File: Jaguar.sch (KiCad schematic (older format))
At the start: 23 parts, among them P1 12v-SW, P10 O2, P11 O2-GND, P12 TACH-IN, P13 Ground, P14 BATT-GND, P15 DIS-BYPASS, P16 IGN-ADVANCE, P17 CONN_4, P18 CONN_4, P19 INJ-GND, P2 BRV-12v, P20 12v-SW, P21 Fuel Relay+, P22 Fuel Relay-, P23 Injectors, P3 BRV-GND, P4 IAT, P5 MAT, P6 COOLANT, P7 TPS-5v, P8 TPS, P9 TPS-GND

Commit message: Redesigned schematics and board
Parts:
- removed P17, P18: CONN_4, symbol CONN_4
- added P15: CAM-IN, symbol CONN_1
- added P2: 12v-SW2, symbol CONN_1
- added P20: PT3-5, symbol CONN_3
- added P21: Inj-IN, symbol CONN_3
- added P3: 12v-SW3, symbol CONN_1
- P14: renamed from P12; value TACH-IN -> CRANK-IN
- P16: renamed from P13; value Ground -> GND
- P17: renamed from P14; value BATT-GND -> GND2
- P23: renamed from P20; value 12v-SW -> 12v-SW4
- P24: renamed from P21; value Fuel Relay+ -> FUEL+
- P25: renamed from P22; value Fuel Relay- -> FUEL-
- P5: renamed from P3; value BRV-GND -> NC
- P9: renamed from P7; value TPS-5v -> NC2
- renumbered P8 to P10, P9 to P11, P10 to P12, P11 to P13, P15 to P18, P16 to P19, P19 to P22, P23 to P26, P2 to P4, P4 to P6, P5 to P7, P6 to P8
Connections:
- net labels added: CAM, ToCPU14
- net labels removed: 5vdc-switch-GND
- no-connect marks 4 -> 6
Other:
- moved on the sheet: P9

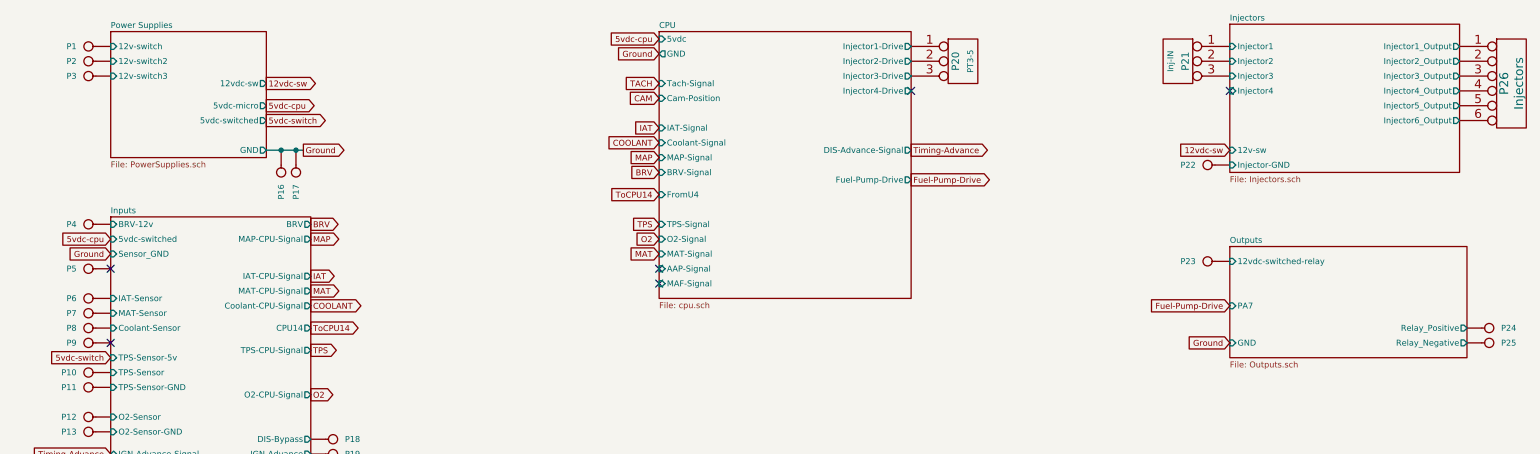
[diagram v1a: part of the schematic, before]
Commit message: Updated Schematics, created new PDF, completed board layout and routing
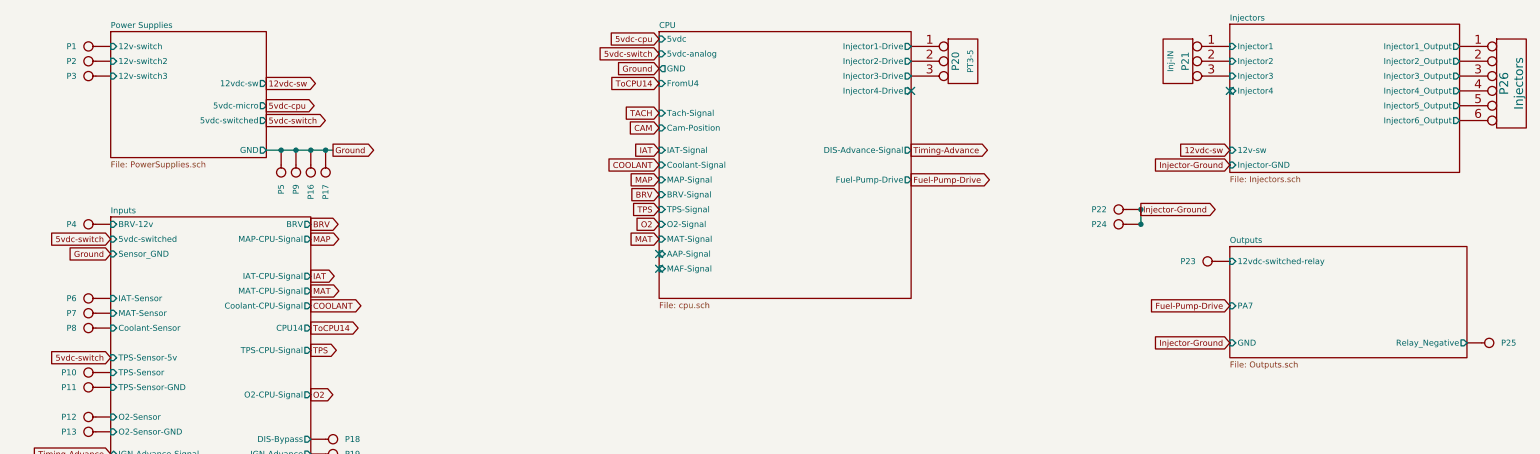
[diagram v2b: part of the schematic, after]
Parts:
- P24: value FUEL+ -> RELAY-GND
- P5: value NC -> Ground
- P9: value NC2 -> Ground
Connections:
- net Outputs/Relay_Positive is gone; now on net Injector-Ground: P24.1
- net Ground: now also P5.1, P9.1
- net Injectors/Injector-GND renamed Injector-Ground
- no-connect marks 6 -> 4
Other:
- moved on the sheet: P16, P17, P22, P24, P5, P9
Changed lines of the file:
@@
-EESchema Schematic File Version 2  date Fri 20 Jan 2012 02:23:37 PM EST
+EESchema Schematic File Version 2  date Sun 22 Jan 2012 12:58:37 AM EST
 LIBS:power
 LIBS:device
@@
 Sheet 1 7
 Title ""
-Date "20 jan 2012"
+Date "22 jan 2012"
 Rev ""
 Comp ""
@@
 Comment4 ""
 $EndDescr
-Text GLabel 5200 1800 0    40   Input ~ 0
+Connection ~ 2950 1500
+Connection ~ 2850 1500
+Wire Wire Line
+	3000 1500 2550 1500
+Connection ~ 8450 1900
+Connection ~ 2650 1500
+Connection ~ 2750 1500
+Wire Wire Line
+	8450 2000 8450 1900
+Connection ~ 8450 2000
+Text GLabel 1500 2100 0    40   Input ~ 0
+5vdc-switch
+Text GLabel 9050 2800 0    40   Input ~ 0
+Injector-Ground
+Text GLabel 9050 1600 0    40   Input ~ 0
+Injector-Ground
+Text GLabel 8450 1900 2    40   Output ~ 0
+Injector-Ground
+Text GLabel 5200 850  0    40   Input ~ 0
+5vdc-switch
+NoConn ~ 5200 2200
+Text GLabel 5200 1050 0    40   Input ~ 0
 ToCPU14
 Text GLabel 2850 2700 2    40   Output ~ 0
 ToCPU14
-NoConn ~ 1500 2300
-NoConn ~ 1500 2800
-Text GLabel 1500 2100 0    40   Input ~ 0
-5vdc-cpu
 NoConn ~ 9050 1100
 $Comp
@@
 	-1   0    0    1
 $EndComp
-Text GLabel 5200 1650 0    40   Input ~ 0
+Text GLabel 5200 1800 0    40   Input ~ 0
 BRV
 NoConn ~ 5200 2300
-Text GLabel 5200 1150 0    40   Input ~ 0
+Text GLabel 5200 1350 0    40   Input ~ 0
 CAM
 Text GLabel 2850 3750 2    40   Output ~ 0
@@
 L CONN_1 P22
 U 1 1 4F125936
-P 8900 1600
-F 0 "P22" H 8980 1600 40  0000 L CNN
-F 1 "INJ-GND" H 8900 1655 30  0001 C CNN
-	1    8900 1600
-	-1   0    0    1
-$EndComp
-Connection ~ 2750 1500
-Wire Wire Line
-	2800 1500 2550 1500
-Connection ~ 2650 1500
+P 8300 1900
+F 0 "P22" H 8380 1900 40  0000 L CNN
+F 1 "INJ-GND" H 8300 1955 30  0001 C CNN
+	1    8300 1900
+	-1   0    0    1
+$EndComp
 $Comp
 L CONN_1 P17
 U 1 1 4F124A8E
-P 2750 1650
-F 0 "P17" H 2830 1650 40  0000 L CNN
-F 1 "GND2" H 2750 1705 30  0001 C CNN
-	1    2750 1650
+P 2950 1650
+F 0 "P17" H 3030 1650 40  0000 L CNN
+F 1 "GND2" H 2950 1705 30  0001 C CNN
+	1    2950 1650
 	0    1    1    0
 $EndComp
@@
 L CONN_1 P16
 U 1 1 4F1248F4
-P 2650 1650
-F 0 "P16" H 2730 1650 40  0000 L CNN
-F 1 "GND" H 2650 1705 30  0001 C CNN
-	1    2650 1650
+P 2850 1650
+F 0 "P16" H 2930 1650 40  0000 L CNN
+F 1 "GND" H 2850 1705 30  0001 C CNN
+	1    2850 1650
 	0    1    1    0
 $EndComp
@@
 L CONN_1 P24
 U 1 1 4F0D845D
-P 10800 2700
-F 0 "P24" H 10880 2700 40  0000 L CNN
-F 1 "FUEL+" H 10800 2755 30  0001 C CNN
-	1    10800 2700
-	1    0    0    -1
-$EndComp
-Text GLabel 9050 2800 0    40   Input ~ 0
-Ground
+P 8300 2000
+F 0 "P24" H 8380 2000 40  0000 L CNN
+F 1 "RELAY-GND" H 8300 2055 30  0001 C CNN
+	1    8300 2000
+	-1   0    0    1
+$EndComp
 $Sheet
 S 9050 2150 1600 750
@@
 F2 "GND" I L 9050 2800 40
 F3 "Relay_Negative" O R 10650 2800 40
-F4 "Relay_Positive" O R 10650 2700 40
-F5 "12vdc-switched-relay" I L 9050 2250 40
-F6 "PA7" I L 9050 2550 40
+F4 "12vdc-switched-relay" I L 9050 2250 40
+F5 "PA7" I L 9050 2550 40
 $EndSheet
 $Comp
@@
 L CONN_1 P5
 U 1 1 4F0C7391
-P 1350 2300
-F 0 "P5" H 1430 2300 40  0000 L CNN
-F 1 "NC" H 1350 2355 30  0001 C CNN
-	1    1350 2300
-	-1   0    0    1
+P 2650 1650
+F 0 "P5" H 2730 1650 40  0000 L CNN
+F 1 "Ground" H 2650 1705 30  0001 C CNN
+	1    2650 1650
+	0    1    1    0
 $EndComp
 $Comp
@@
 L CONN_1 P9
 U 1 1 4F0BB54E
-P 1350 2800
-F 0 "P9" H 1430 2800 40  0000 L CNN
-F 1 "NC2" H 1350 2855 30  0001 C CNN
-	1    1350 2800
-	-1   0    0    1
+P 2750 1650
+F 0 "P9" H 2830 1650 40  0000 L CNN
+F 1 "Ground" H 2750 1705 30  0001 C CNN
+	1    2750 1650
+	0    1    1    0
 $EndComp
 $Comp
@@
 Text GLabel 1500 3550 0    40   Input ~ 0
 Timing-Advance
-Text GLabel 5200 2100 0    40   Input ~ 0
+Text GLabel 5200 2000 0    40   Input ~ 0
 O2
 Text GLabel 2850 3150 2    40   Output ~ 0
 O2
-Text GLabel 5200 2000 0    40   Input ~ 0
+Text GLabel 5200 1900 0    40   Input ~ 0
 TPS
 Text GLabel 2850 2850 2    40   Output ~ 0
 TPS
-Text GLabel 5200 1450 0    40   Input ~ 0
+Text GLabel 5200 1600 0    40   Input ~ 0
 COOLANT
 Text GLabel 2850 2550 2    40   Output ~ 0
 COOLANT
-Text GLabel 5200 2200 0    40   Input ~ 0
+Text GLabel 5200 2100 0    40   Input ~ 0
 MAT
 Text GLabel 2850 2450 2    40   Output ~ 0
 MAT
-Text GLabel 5200 1350 0    40   Input ~ 0
+Text GLabel 5200 1500 0    40   Input ~ 0
 IAT
 Text GLabel 2850 2350 2    40   Output ~ 0
@@
 Text GLabel 6900 1500 2    40   Output ~ 0
 Timing-Advance
-Text GLabel 5200 1050 0    40   Input ~ 0
+Text GLabel 5200 1250 0    40   Input ~ 0
 TACH
-Text GLabel 5200 1550 0    40   Input ~ 0
+Text GLabel 5200 1700 0    40   Input ~ 0
 MAP
-NoConn ~ 5200 2400
 Text GLabel 5200 750  0    40   Input ~ 0
 5vdc-cpu
-Text GLabel 5200 850  0    40   Input ~ 0
+Text GLabel 5200 950  0    40   Input ~ 0
 Ground
-Text GLabel 2800 1500 2    40   Output ~ 0
+Text GLabel 3000 1500 2    40   Output ~ 0
 Ground
 Text GLabel 2550 1200 2    40   Output ~ 0
@@
 F1 "cpu.sch" 40
 F2 "5vdc" I L 5200 750 40
-F3 "GND" O L 5200 850 40
+F3 "GND" O L 5200 950 40
 F4 "Fuel-Pump-Drive" O R 6900 1700 40
 F5 "Injector4-Drive" O R 6900 1100 40
@@
 F8 "Injector1-Drive" O R 6900 800 40
 F9 "DIS-Advance-Signal" O R 6900 1500 40
-F10 "Tach-Signal" I L 5200 1050 40
-F11 "MAF-Signal" I L 5200 2400 40
-F12 "MAT-Signal" I L 5200 2200 40
-F13 "BRV-Signal" I L 5200 1650 40
-F14 "MAP-Signal" I L 5200 1550 40
-F15 "O2-Signal" I L 5200 2100 40
-F16 "TPS-Signal" I L 5200 2000 40
-F17 "Coolant-Signal" I L 5200 1450 40
-F18 "IAT-Signal" I L 5200 1350 40
-F19 "AAP-Signal" I L 5200 2300 40
-F20 "Cam-Position" I L 5200 1150 40
-F21 "FromU4" I L 5200 1800 40
+F10 "Tach-Signal" I L 5200 1250 40
+F11 "MAF-Signal" I L 5200 2300 40
+F12 "MAT-Signal" I L 5200 2100 40
+F13 "BRV-Signal" I L 5200 1800 40
+F14 "MAP-Signal" I L 5200 1700 40
+F15 "O2-Signal" I L 5200 2000 40
+F16 "TPS-Signal" I L 5200 1900 40
+F17 "Coolant-Signal" I L 5200 1600 40
+F18 "IAT-Signal" I L 5200 1500 40
+F19 "AAP-Signal" I L 5200 2200 40
+F20 "Cam-Position" I L 5200 1350 40
+F21 "FromU4" I L 5200 1050 40
+F22 "5vdc-analog" I L 5200 850 40
 $EndSheet
 $EndSCHEMATC

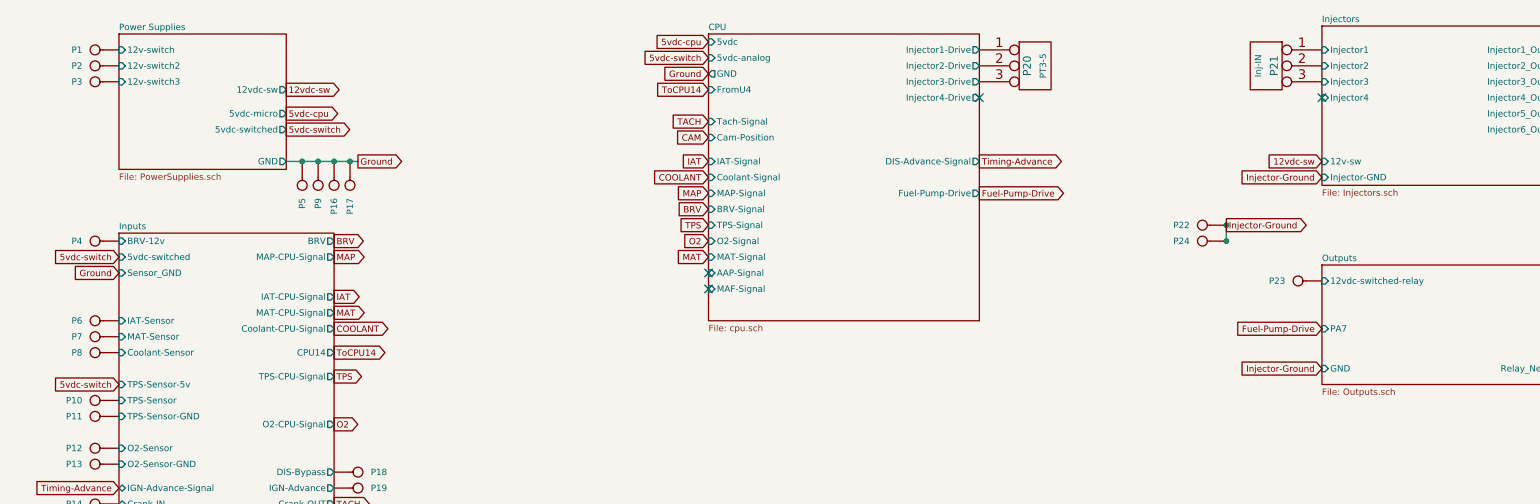
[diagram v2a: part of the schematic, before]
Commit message: Modified: schematics to correct errors
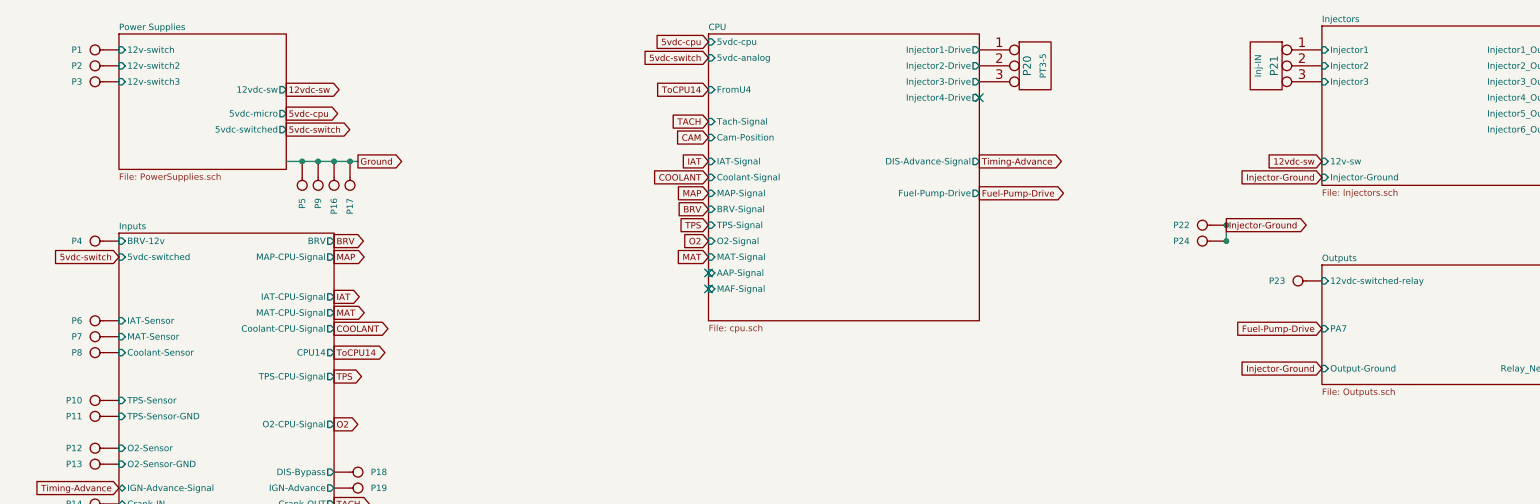
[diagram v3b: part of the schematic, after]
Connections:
- no-connect marks 4 -> 3
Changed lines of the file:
@@
-EESchema Schematic File Version 2  date Sun 22 Jan 2012 12:58:37 AM EST
+EESchema Schematic File Version 2  date Sun 22 Jan 2012 05:59:51 PM EST
 LIBS:power
 LIBS:device
@@
 Comment4 ""
 $EndDescr
+$Sheet
+S 1500 1950 1350 1900
+U 4F0BB08D
+F0 "Inputs" 40
+F1 "inputs.sch" 40
+F2 "DIS-Bypass" O R 2850 3450 40
+F3 "O2-Sensor-GND" I L 1500 3400 40
+F4 "TPS-Sensor-GND" I L 1500 3100 40
+F5 "Coolant-Sensor" I L 1500 2700 40
+F6 "Coolant-CPU-Signal" O R 2850 2550 40
+F7 "O2-Sensor" I L 1500 3300 40
+F8 "O2-CPU-Signal" O R 2850 3150 40
+F9 "IAT-CPU-Signal" O R 2850 2350 40
+F10 "IAT-Sensor" I L 1500 2500 40
+F11 "TPS-CPU-Signal" O R 2850 2850 40
+F12 "TPS-Sensor" I L 1500 3000 40
+F13 "MAT-Sensor" I L 1500 2600 40
+F14 "MAT-CPU-Signal" O R 2850 2450 40
+F15 "BRV" O R 2850 2000 40
+F16 "MAP-CPU-Signal" O R 2850 2100 40
+F17 "5vdc-switched" I L 1500 2100 40
+F18 "IGN-Advance-Signal" B L 1500 3550 40
+F19 "IGN-Advance" O R 2850 3550 40
+F20 "BRV-12v" I L 1500 2000 40
+F21 "CamPosition-IN" B L 1500 3750 40
+F22 "CamPosition-OUT" B R 2850 3750 40
+F23 "Crank-OUT" O R 2850 3650 40
+F24 "Crank-IN" B L 1500 3650 40
+F25 "CPU14" O R 2850 2700 40
+$EndSheet
 Connection ~ 2950 1500
 Connection ~ 2850 1500
@@
 Text GLabel 2850 2700 2    40   Output ~ 0
 ToCPU14
-NoConn ~ 9050 1100
 $Comp
 L CONN_3 P21
@@
 F0 "Outputs" 40
 F1 "Outputs.sch" 40
-F2 "GND" I L 9050 2800 40
-F3 "Relay_Negative" O R 10650 2800 40
-F4 "12vdc-switched-relay" I L 9050 2250 40
-F5 "PA7" I L 9050 2550 40
+F2 "Relay_Negative" O R 10650 2800 40
+F3 "12vdc-switched-relay" I L 9050 2250 40
+F4 "PA7" I L 9050 2550 40
+F5 "Output-Ground" I L 9050 2800 40
 $EndSheet
 $Comp
@@
 F2 "Injector6_Output" O R 10600 1300 40
 F3 "Injector5_Output" O R 10600 1200 40
-F4 "Injector4" I L 9050 1100 40
-F5 "Injector4_Output" O R 10600 1100 40
-F6 "Injector3_Output" O R 10600 1000 40
-F7 "Injector3" I L 9050 1000 40
-F8 "Injector2" I L 9050 900 40
-F9 "Injector2_Output" O R 10600 900 40
-F10 "Injector1_Output" O R 10600 800 40
-F11 "Injector1" I L 9050 800 40
-F12 "Injector-GND" I L 9050 1600 40
-F13 "12v-sw" I L 9050 1500 40
+F4 "Injector4_Output" O R 10600 1100 40
+F5 "Injector3_Output" O R 10600 1000 40
+F6 "Injector3" I L 9050 1000 40
+F7 "Injector2" I L 9050 900 40
+F8 "Injector2_Output" O R 10600 900 40
+F9 "Injector1_Output" O R 10600 800 40
+F10 "Injector1" I L 9050 800 40
+F11 "12v-sw" I L 9050 1500 40
+F12 "Injector-Ground" I L 9050 1600 40
 $EndSheet
 $Sheet
@@
 F0 "Power Supplies" 40
 F1 "PowerSupplies.sch" 40
-F2 "GND" O R 2550 1500 40
-F3 "5vdc-switched" O R 2550 1300 40
-F4 "12v-switch" I L 1500 800 40
-F5 "12vdc-sw" O R 2550 1050 40
-F6 "5vdc-micro" O R 2550 1200 40
-F7 "12v-switch3" I L 1500 1000 40
-F8 "12v-switch2" I L 1500 900 40
+F2 "5vdc-switched" O R 2550 1300 40
+F3 "12v-switch" I L 1500 800 40
+F4 "12vdc-sw" O R 2550 1050 40
+F5 "5vdc-micro" O R 2550 1200 40
+F6 "12v-switch3" I L 1500 1000 40
+F7 "12v-switch2" I L 1500 900 40
 $EndSheet
 $Comp
@@
 Text GLabel 2850 2000 2    40   Output ~ 0
 BRV
-Text GLabel 1500 2200 0    40   Input ~ 0
-Ground
-Text GLabel 1500 2900 0    40   Input ~ 0
-5vdc-switch
-$Sheet
-S 1500 1950 1350 1900
-U 4F0BB08D
-F0 "Inputs" 40
-F1 "inputs.sch" 40
-F2 "DIS-Bypass" O R 2850 3450 40
-F3 "O2-Sensor-GND" I L 1500 3400 40
-F4 "TPS-Sensor-GND" I L 1500 3100 40
-F5 "TPS-Sensor-5v" I L 1500 2900 40
-F6 "Coolant-Sensor" I L 1500 2700 40
-F7 "Coolant-CPU-Signal" O R 2850 2550 40
-F8 "O2-Sensor" I L 1500 3300 40
-F9 "O2-CPU-Signal" O R 2850 3150 40
-F10 "IAT-CPU-Signal" O R 2850 2350 40
-F11 "IAT-Sensor" I L 1500 2500 40
-F12 "TPS-CPU-Signal" O R 2850 2850 40
-F13 "TPS-Sensor" I L 1500 3000 40
-F14 "MAT-Sensor" I L 1500 2600 40
-F15 "MAT-CPU-Signal" O R 2850 2450 40
-F16 "BRV" O R 2850 2000 40
-F17 "MAP-CPU-Signal" O R 2850 2100 40
-F18 "5vdc-switched" I L 1500 2100 40
-F19 "IGN-Advance-Signal" B L 1500 3550 40
-F20 "IGN-Advance" O R 2850 3550 40
-F21 "Sensor_GND" I L 1500 2200 40
-F22 "BRV-12v" I L 1500 2000 40
-F23 "CamPosition-IN" B L 1500 3750 40
-F24 "CamPosition-OUT" B R 2850 3750 40
-F25 "Crank-OUT" O R 2850 3650 40
-F26 "Crank-IN" B L 1500 3650 40
-F27 "CPU14" O R 2850 2700 40
-$EndSheet
 Text GLabel 6900 1500 2    40   Output ~ 0
 Timing-Advance
@@
 Text GLabel 5200 750  0    40   Input ~ 0
 5vdc-cpu
-Text GLabel 5200 950  0    40   Input ~ 0
-Ground
 Text GLabel 3000 1500 2    40   Output ~ 0
 Ground
@@
 F0 "CPU" 40
 F1 "cpu.sch" 40
-F2 "5vdc" I L 5200 750 40
-F3 "GND" O L 5200 950 40
-F4 "Fuel-Pump-Drive" O R 6900 1700 40
-F5 "Injector4-Drive" O R 6900 1100 40
-F6 "Injector3-Drive" O R 6900 1000 40
-F7 "Injector2-Drive" O R 6900 900 40
-F8 "Injector1-Drive" O R 6900 800 40
-F9 "DIS-Advance-Signal" O R 6900 1500 40
-F10 "Tach-Signal" I L 5200 1250 40
-F11 "MAF-Signal" I L 5200 2300 40
-F12 "MAT-Signal" I L 5200 2100 40
-F13 "BRV-Signal" I L 5200 1800 40
-F14 "MAP-Signal" I L 5200 1700 40
-F15 "O2-Signal" I L 5200 2000 40
-F16 "TPS-Signal" I L 5200 1900 40
-F17 "Coolant-Signal" I L 5200 1600 40
-F18 "IAT-Signal" I L 5200 1500 40
-F19 "AAP-Signal" I L 5200 2200 40
-F20 "Cam-Position" I L 5200 1350 40
-F21 "FromU4" I L 5200 1050 40
-F22 "5vdc-analog" I L 5200 850 40
+F2 "Fuel-Pump-Drive" O R 6900 1700 40
+F3 "Injector4-Drive" O R 6900 1100 40
+F4 "Injector3-Drive" O R 6900 1000 40
+F5 "Injector2-Drive" O R 6900 900 40
+F6 "Injector1-Drive" O R 6900 800 40
+F7 "DIS-Advance-Signal" O R 6900 1500 40
+F8 "Tach-Signal" I L 5200 1250 40
+F9 "MAF-Signal" I L 5200 2300 40
+F10 "MAT-Signal" I L 5200 2100 40
+F11 "BRV-Signal" I L 5200 1800 40
+F12 "MAP-Signal" I L 5200 1700 40
+F13 "O2-Signal" I L 5200 2000 40
+F14 "TPS-Signal" I L 5200 1900 40
+F15 "Coolant-Signal" I L 5200 1600 40
+F16 "IAT-Signal" I L 5200 1500 40
+F17 "AAP-Signal" I L 5200 2200 40
+F18 "Cam-Position" I L 5200 1350 40
+F19 "FromU4" I L 5200 1050 40
+F20 "5vdc-analog" I L 5200 850 40
+F21 "5vdc-cpu" I L 5200 750 40
 $EndSheet
 $EndSCHEMATC
